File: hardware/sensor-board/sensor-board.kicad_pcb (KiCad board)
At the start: 4 copper layers, 47.2 x 26.5 mm, 32 parts, among them J1 QWIIC Connector, J2 QWIIC Connector, J3 Vin Connector, J4 1x3 connector, Q1 BSS84, U2 DS2482S-100+, U3 LMV601, U4 MCP96L01T-E/MX, U5 ADS7823EB/250

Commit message: v1.0 of qwiic interface board layout
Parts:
- added G***: LOGO, Beirdo:qwiic-logo, B.Cu at (98.5, 148.7)
- added REF**: OSHW-Logo2_7.3x6mm_SilkScreen, Symbol:OSHW-Logo2_7.3x6mm_SilkScreen, B.Cu at (111.4, 147.1)

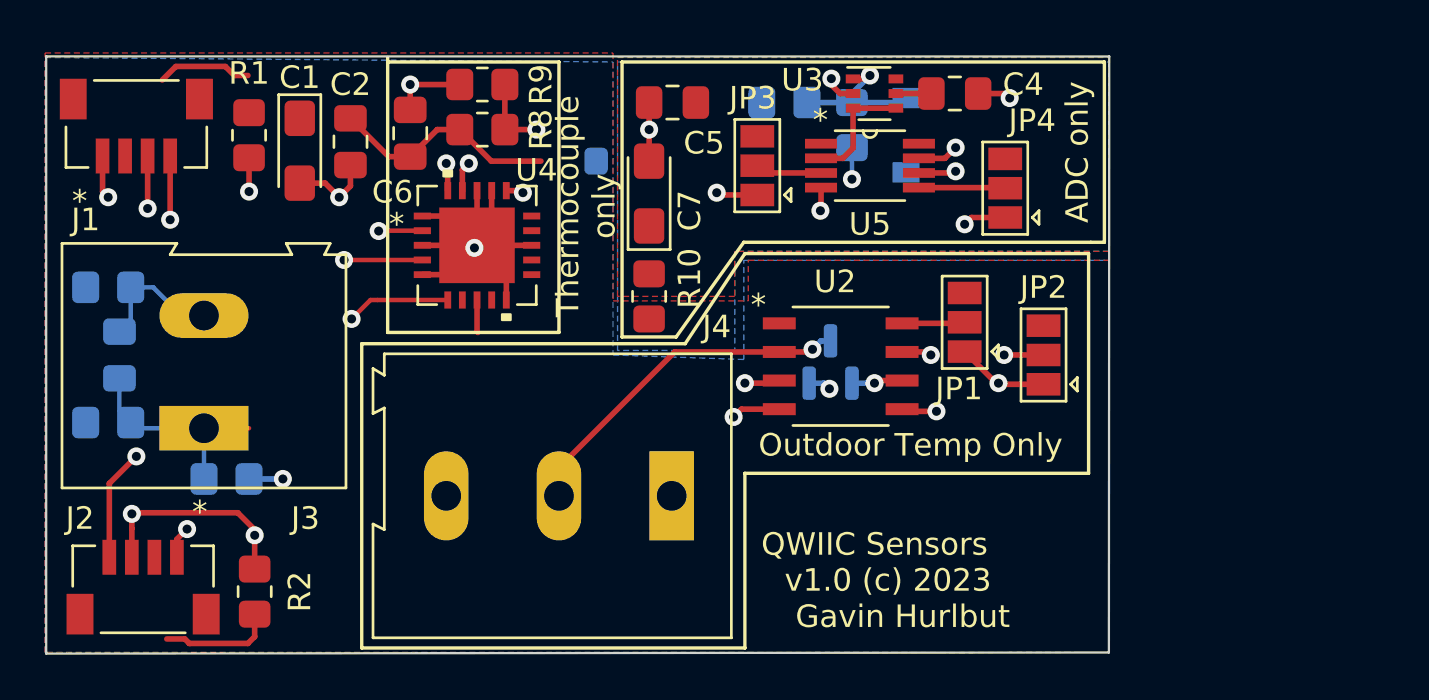
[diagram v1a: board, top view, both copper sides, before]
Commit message: Added GPIO/EEPROM on sensor board
- this will allow me to connect the ignition wire, and also to have the
  boards report their capabilities to the firmware
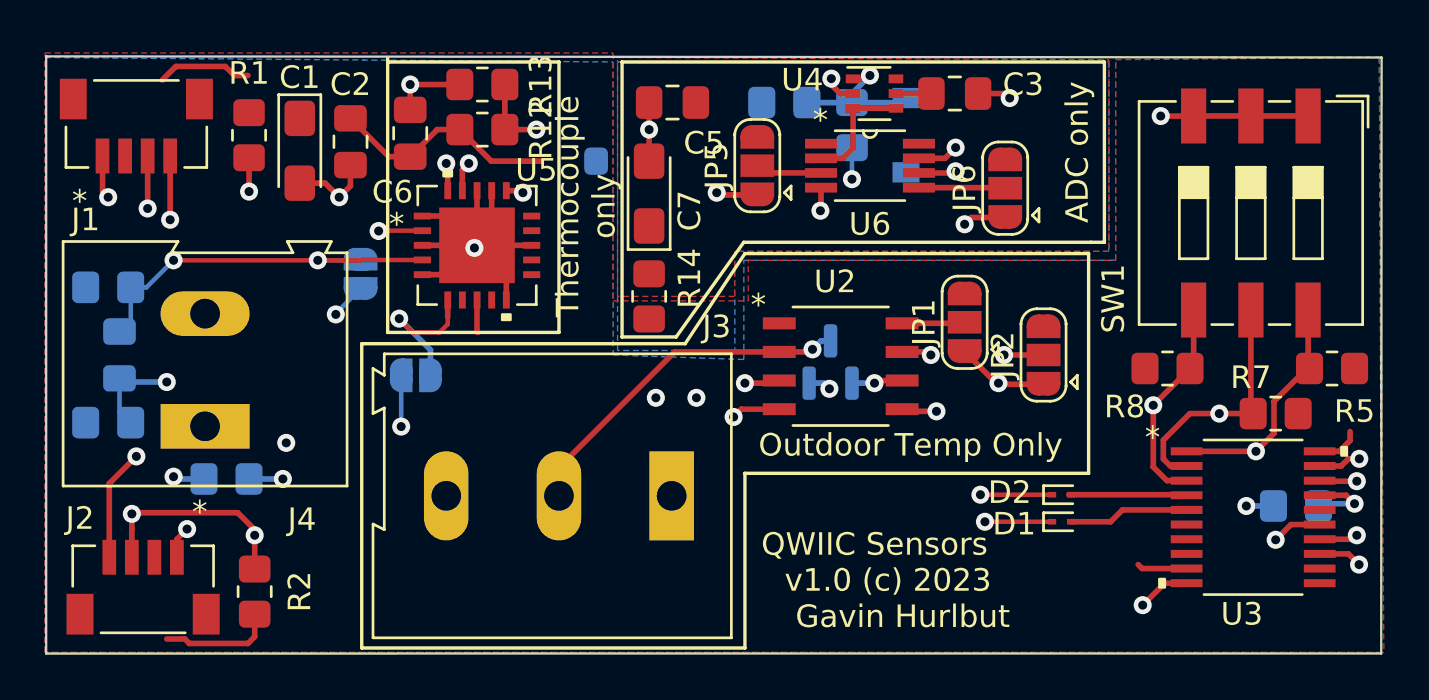
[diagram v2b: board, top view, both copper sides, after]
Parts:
- removed the J3 at (82.2, 141.2)
- removed the REF** at (111.4, 147.1)
- added D1: ACDBQC0130L-HF, Diode_SMD:D_SOD-923, F.Cu at (120.3, 145.4)
- added D2: ACDBQC0130L-HF, Diode_SMD:D_SOD-923, F.Cu at (120.3, 144.2)
- added J4: 2-pole terminal, TerminalBlock:TerminalBlock_Altech_AK300-2_P5.00mm, F.Cu at (82.3, 141.2)
- added JP3: Solder Jumper, Jumper:SolderJumper-2_P1.3mm_Open_RoundedPad1.0x1.5mm, B.Cu at (91.7, 138.9)
- added JP4: Solder Jumper, Jumper:SolderJumper-2_P1.3mm_Open_RoundedPad1.0x1.5mm, B.Cu at (89.2, 134.4)
- added R3: 10k, Resistor_SMD:R_0805_2012Metric_Pad1.20x1.40mm_HandSolder, B.Cu at (130.7, 144.7)
- added R5: 10k, Resistor_SMD:R_0805_2012Metric_Pad1.20x1.40mm_HandSolder, F.Cu at (132.3, 138.6)
- added R7: 10k, Resistor_SMD:R_0805_2012Metric_Pad1.20x1.40mm_HandSolder, F.Cu at (129.8, 140.6)
- added R8: 10k, Resistor_SMD:R_0805_2012Metric_Pad1.20x1.40mm_HandSolder, F.Cu at (125.0, 138.6)
- added REF**: OSHW-Logo2_9.8x8mm_SilkScreen, Symbol:OSHW-Logo2_9.8x8mm_SilkScreen, B.Cu at (112.1, 147.3)
- added SW1: SW_DIP_x03, Button_Switch_SMD:SW_DIP_SPSTx03_Slide_9.78x9.8mm_W8.61mm_P2.54mm, F.Cu at (128.7, 131.7)
- added U3: PCA9501PW_118, UltraLibrarian:PCA9501PW_118, F.Cu at (128.8, 145.2)
- J3: renamed from J4; value 1x3 connector -> 3-pole terminal
- JP1, JP2: footprint Jumper:SolderJumper-3_P1.3mm_Open_Pad1.0x1.5mm -> Jumper:SolderJumper-3_P1.3mm_Open_RoundedPad1.0x1.5mm
- JP5: renamed from JP3; footprint Jumper:SolderJumper-3_P1.3mm_Open_Pad1.0x1.5mm -> Jumper:SolderJumper-3_P1.3mm_Open_RoundedPad1.0x1.5mm
- JP6: renamed from JP4; footprint Jumper:SolderJumper-3_P1.3mm_Open_Pad1.0x1.5mm -> Jumper:SolderJumper-3_P1.3mm_Open_RoundedPad1.0x1.5mm
- renumbered C4 to C3, C3 to C4, D1 to D3, R6 to R10, R7 to R11, R8 to R12, R9 to R13, R10 to R14, R3 to R4, R4 to R6, R5 to R9, U3 to U4, U4 to U5, U5 to U6
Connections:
- net VIN- renamed Net-(C4-Pad2)
- C4 pad 1: VIN+ -> Net-(C4-Pad1)
- R10 pad 1: VIN+ -> Net-(C4-Pad1)
- R9 pad 2: VIN+ -> Net-(C4-Pad1)
- U5 pad 2: VIN+ -> Net-(C4-Pad1)
- U5 pad 6: VIN+ -> Net-(C4-Pad1)
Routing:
- net VIN-: track 0.00 -> 42.6 mm, vias 0 -> 3
- net Net-(C4-Pad1): track 0.00 -> 35.3 mm, vias 0 -> 4
- net SCL: track 82.9 -> 114.2 mm, vias 6 -> 8
- net SDA: track 89.8 -> 111.7 mm, vias 6 -> 7
- net A1: track 0.00 -> 21.3 mm, vias 0 -> 2
- net A2: track 0.00 -> 20.5 mm, vias 0 -> 2
- net A0: track 0.00 -> 19.3 mm, vias 0 -> 2
- net GND: track 35.0 -> 43.9 mm, vias 7 -> 9
- net VIN+: track 65.3 -> 57.5 mm, vias 3 -> 4
- net +3V3: track 23.5 -> 28.9 mm, vias 2 -> 3
- net Net-(D1-Pad2): track 0.00 -> 5.34 mm
- net Net-(D2-Pad2): track 0.00 -> 5.24 mm
- net Net-(R3-Pad2): track 0.00 -> 3.34 mm, vias 0 -> 1
- net Net-(C4-Pad2): track 16.6 -> 17.5 mm, vias 1 -> 2
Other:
- board size 47.2 x 26.5 mm -> 59.2 x 26.5 mm

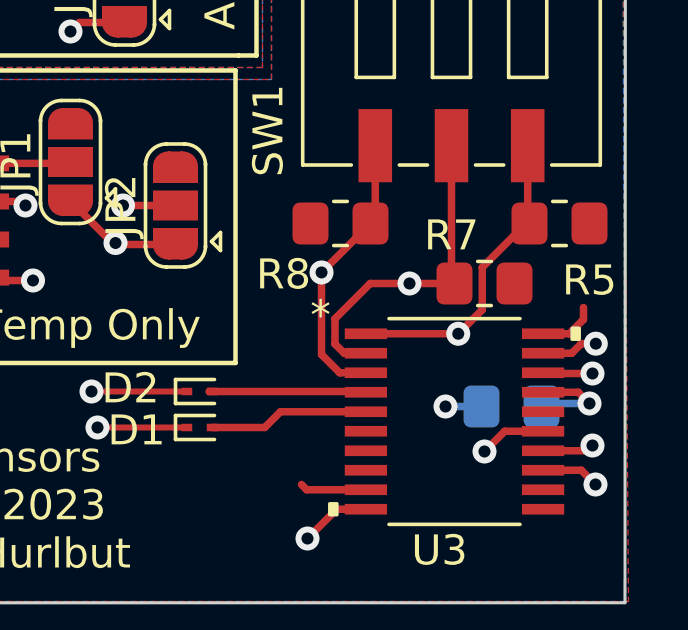
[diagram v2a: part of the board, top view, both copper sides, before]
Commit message: Added logging, added debug serial to mainboard
- also added eeprom read support, and the digital GPIO over I2C
- route the ignition wire as a digital GPIO so we can use it as an input
  to the state machine.
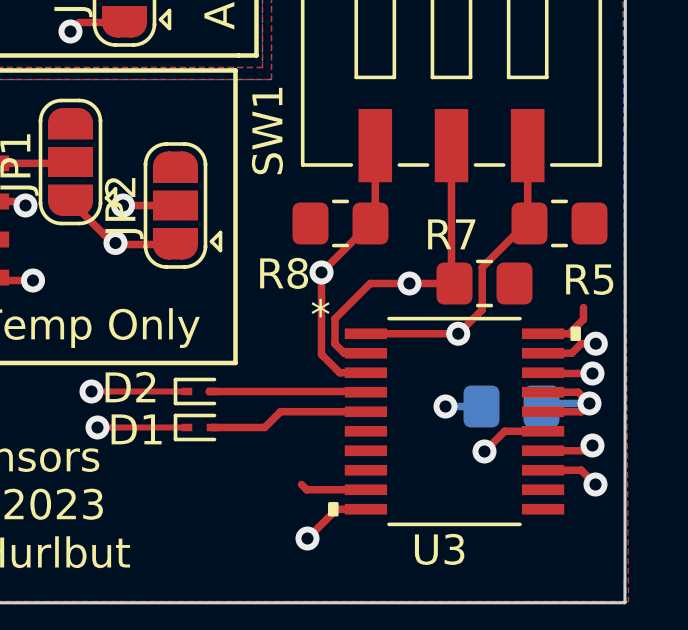
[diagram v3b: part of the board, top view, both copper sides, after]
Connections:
- R3 pad 2: Net-(R3-Pad2) -> Net-(U3-Pad17)
- U3 pad 16: unconnected-(U3-Pad16) -> Net-(U3-Pad17)
- U3 pad 17: Net-(R3-Pad2) -> Net-(U3-Pad17)
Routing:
- net Net-(U3-Pad17): track 0.00 -> 5.01 mm, vias 0 -> 1
- net Net-(R3-Pad2): track 3.34 -> 0.00 mm, vias 1 -> 0

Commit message: Changed solder pad style, added in the Sensor EEPROM init
- of course, no boards hooked up yet, so it properly detects it.
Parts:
- JP1, JP2, JP5, JP6: footprint Jumper:SolderJumper-3_P1.3mm_Open_RoundedPad1.0x1.5mm -> Jumper:SolderJumper-3_P2.0mm_Open_TrianglePad1.0x1.5mm
- JP3, JP4: footprint Jumper:SolderJumper-2_P1.3mm_Open_RoundedPad1.0x1.5mm -> Jumper:SolderJumper-2_P1.3mm_Open_TrianglePad1.0x1.5mm
- moved JP6 1.12 mm to (118.8, 130.1)
- moved JP3 1.03 mm to (90.6, 138.9)
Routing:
- net +3V3A: track 1.58 -> 4.48 mm
- net Net-(JP6-Pad2): track 3.84 -> 5.11 mm
- net GND: track 43.9 -> 44.6 mm
